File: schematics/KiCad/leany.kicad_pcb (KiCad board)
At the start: 2 copper layers, 108.3 x 71.6 mm, 61 parts, among them J1 SWD, J2 ST7735S, J3 USB C, Q1 AO3401A, Q2 DMG6601LVT-7, SW1 BOOT_MODE, SW2 ZERO, SW3 HOLD, SW4 POWER, U1 LSM6DSO, U2 STM32F103C8Tx, U3 CH340C, U4 AP2112K-3.3, U5 BQ25619, Y1 8MHz

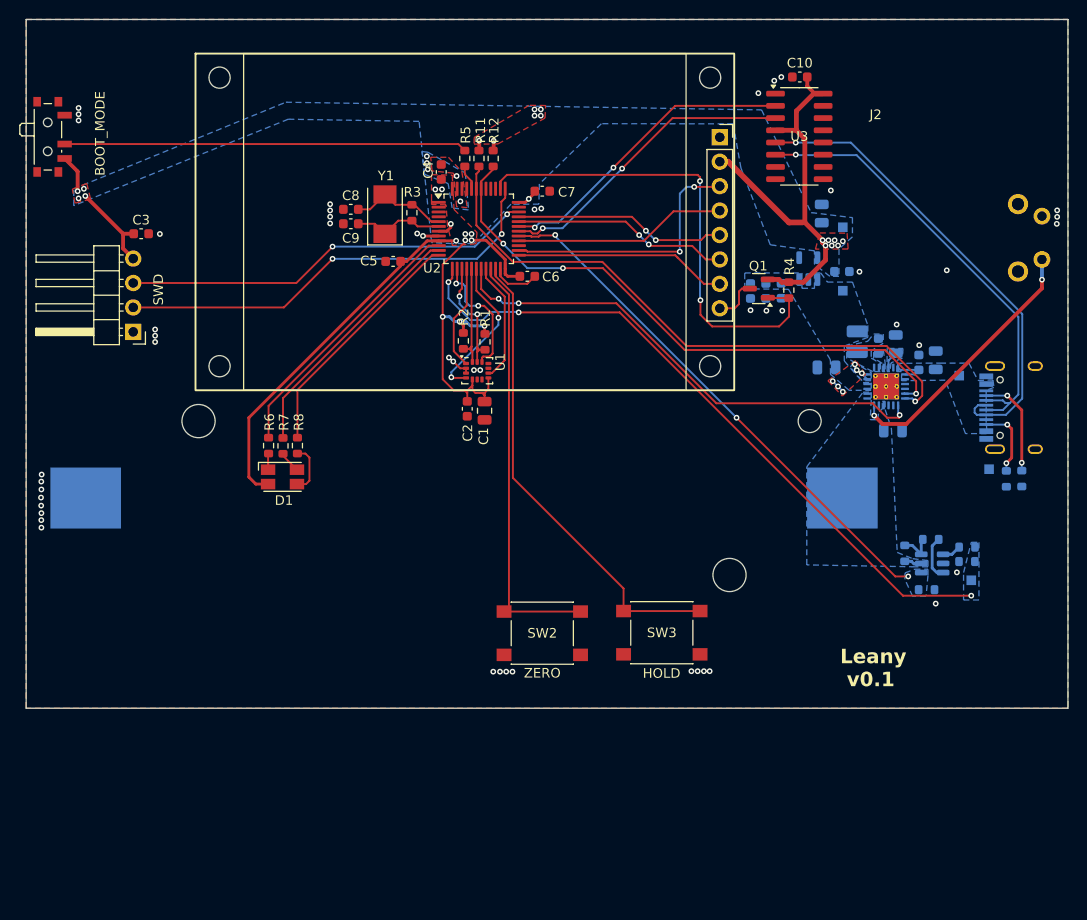
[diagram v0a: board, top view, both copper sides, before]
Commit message: redesign layout and power management
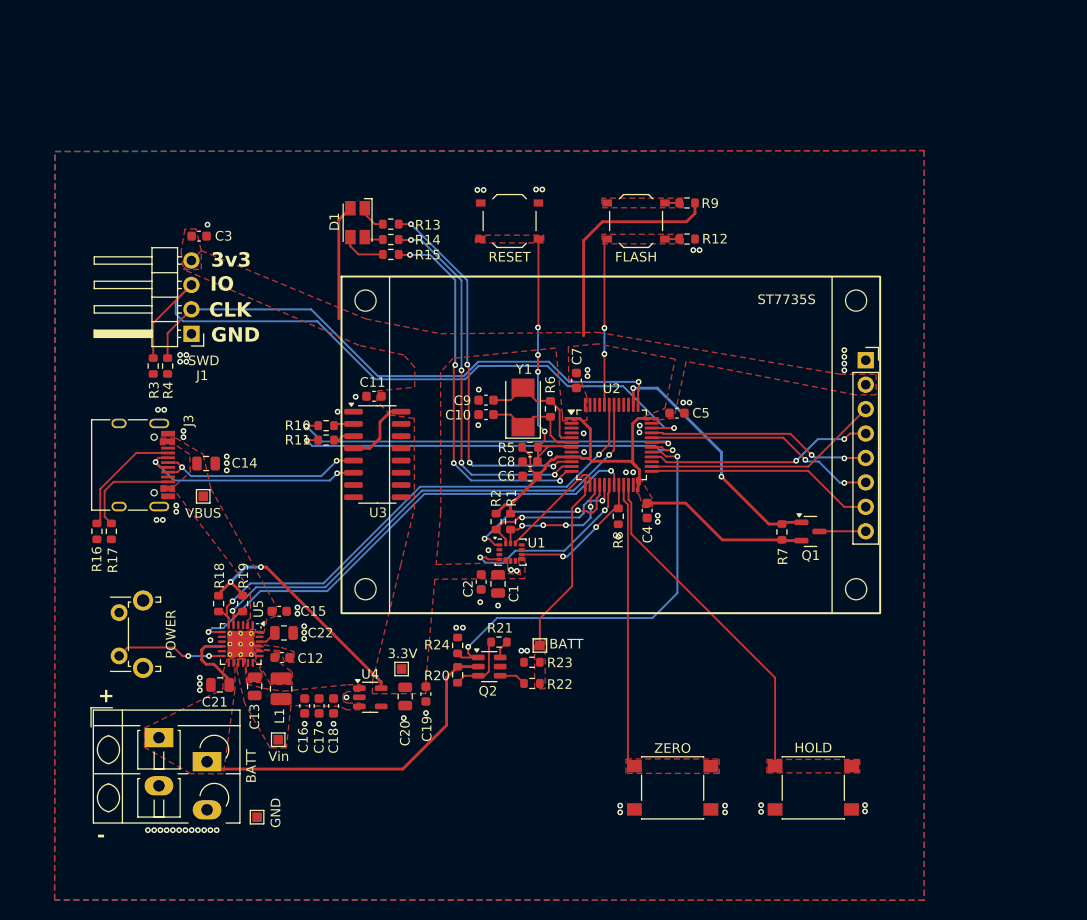
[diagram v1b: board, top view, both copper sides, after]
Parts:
- removed BT1: Battery, Battery:BatteryHolder_Keystone_1042_1x18650
- added C22: 4.7u, Capacitor_SMD:C_0805_2012Metric, F.Cu at (116.2, 119.8)
- added J4: BATT, TerminalBlock_WAGO:TerminalBlock_WAGO_804-102_1x02_P5.00mm_45Degree, F.Cu at (103.2, 130.7)
- added R18: 4.7k, Resistor_SMD:R_0603_1608Metric, F.Cu at (109.5, 116.8)
- added R19: 4.7k, Resistor_SMD:R_0603_1608Metric, F.Cu at (112.0, 116.8)
- added R20: 10k, Resistor_SMD:R_0603_1608Metric, F.Cu at (134.3, 124.2)
- added R21: 10k, Resistor_SMD:R_0603_1608Metric, F.Cu at (138.6, 120.8)
- added R22: 56k, Resistor_SMD:R_0603_1608Metric, F.Cu at (142.0, 125.0)
- added R23: 56k, Resistor_SMD:R_0603_1608Metric, F.Cu at (142.0, 122.8)
- added R24: 100k, Resistor_SMD:R_0603_1608Metric, F.Cu at (134.3, 121.1)
- added SW5: POWER, Button_Switch_THT:SW_Tactile_SPST_Angled_PTS645Vx31-2LFS, F.Cu at (99.1, 122.2)
- C10: value 100n -> 20p
- C11: value 47n -> 100n; moved to F.Cu
- C12: value 10u -> 47n; footprint Capacitor_SMD:C_0805_2012Metric -> Capacitor_SMD:C_0603_1608Metric; moved to F.Cu
- C13: value 22u -> 10u; moved to F.Cu
- C14: value 1u -> 22u; footprint Capacitor_SMD:C_0603_1608Metric -> Capacitor_SMD:C_0805_2012Metric; moved to F.Cu
- C15: value 22n -> 1u; moved to F.Cu
- C16: value 100n -> 22n; moved to F.Cu
- C17: value 1u -> 100n; moved to F.Cu
- C18, C20, J3, L1, Q2, TP1, TP2, TP3, TP4, U4, U5: moved to F.Cu
- C19: value 10u -> 1u; footprint Capacitor_SMD:C_0805_2012Metric -> Capacitor_SMD:C_0603_1608Metric; moved to F.Cu
- C21: value 4.7u -> 10u; moved to F.Cu
- C8: value 20p -> 1u
- R10: value 5.1k -> 4k7; moved to F.Cu
- R11: value 4.7k -> 4k7
- R12: value 4.7k -> 100k
- R13, R14: value 10k -> 820R; moved to F.Cu
- R15: value 56k -> 820R; moved to F.Cu
- R16: value 56k -> 5.1k; moved to F.Cu
- R17: value 100k -> 5.1k; moved to F.Cu
- R3: value 1M -> 10k
- R4: value 18k -> 10k
- R5: value 100k -> 10k
- R6: value 820R -> 1M
- R7: value 820R -> 18k
- R8: value 820R -> 100k
- R9: value 5.1k -> 10k; moved to F.Cu
- SW1: value BOOT_MODE -> RESET; footprint Button_Switch_SMD:SW_SPDT_PCM12 -> Button_Switch_SMD:SW_Push_1P1T_XKB_TS-1187A
- SW2: value ZERO -> FLASH; footprint leany_footprints:SW_Push_1P1T_NO_6x6mm_H9.5mm -> Button_Switch_SMD:SW_Push_1P1T_XKB_TS-1187A
- SW3: value HOLD -> ZERO
- SW4: value POWER -> HOLD; footprint Button_Switch_THT:SW_Tactile_SPST_Angled_PTS645Vx31-2LFS -> leany_footprints:SW_Push_1P1T_NO_6x6mm_H9.5mm; moved to F.Cu
- TP5: value BATT+ -> BATT; moved to F.Cu
- moved J3 93.3 mm to (100.2, 102.3)
- moved R16 90.5 mm to (96.8, 109.2), turned to -90 degrees
- moved R17 85.0 mm to (98.3, 109.2), turned to -90 degrees
- moved TP4 84.3 mm to (113.5, 138.9), turned to 0 degrees
- moved TP2 79.6 mm to (107.8, 105.6), turned to 0 degrees
- moved C21 78.7 mm to (109.6, 125.2), turned to 180 degrees
- moved C13 78.5 mm to (113.2, 125.3)
- moved TP1 75.0 mm to (115.7, 130.9), turned to 0 degrees
- moved C14 74.8 mm to (108.2, 102.2), turned to 0 degrees
- moved U5 72.2 mm to (111.8, 121.0), turned to -90 degrees
- moved R10 70.9 mm to (120.6, 98.2), turned to 0 degrees
- moved L1 69.9 mm to (116.0, 125.6), turned to -90 degrees
- moved C18 69.5 mm to (121.4, 127.4), turned to -90 degrees
- moved R15 67.2 mm to (127.3, 80.5), turned to 0 degrees
- moved R4 65.1 mm to (104.2, 92.0), turned to -90 degrees
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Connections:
- C10 pad 1: +3V3 -> GND
- C10 pad 2: GND -> Net-(U2-PD1)
- C11 pad 1: Net-(C11-Pad1) -> +3V3
- C11 pad 2: Net-(U5-BTST) -> GND
- C12 pad 1: SYS -> Net-(C12-Pad1)
- C12 pad 2: GND -> Net-(U5-BTST)
- C13 pad 1: Net-(U5-PSEL) -> SYS
- C15 pad 1: SYS -> Net-(U5-PSEL)
- C18 pad 1: +3V3 -> SYS
- C20 pad 1: +BATT -> +3V3
- C21 pad 1: Net-(U5-REGN) -> +BATT
- C8 pad 2: Net-(U2-PD0) -> Net-(U2-NRST)
- C9 pad 2: Net-(U2-PD1) -> Net-(U2-PD0)
- L1 pad 1: Net-(C11-Pad1) -> Net-(C12-Pad1)
- R10 pad 1: Net-(J3-CC2) -> /FTDI_RX
- R10 pad 2: GND -> Net-(U3-TXD)
- R11 pad 1: CHG_SDA -> /FTDI_TX
- R11 pad 2: +3V3 -> Net-(U3-RXD)
- R12 pad 1: CHG_SCL -> /BOOT0
- R12 pad 2: +3V3 -> GND
- R13 pad 1: Net-(Q2B-G) -> Net-(D1-RK)
- R13 pad 2: +BATT -> /LED_RED
- R14 pad 1: Net-(Q2B-G) -> Net-(D1-GK)
- R14 pad 2: Net-(Q2A-D) -> /LED_GREEN
- R15 pad 1: BATT_VOLT -> Net-(D1-BK)
- R15 pad 2: Net-(Q2B-D) -> /LED_BLUE
- R16 pad 1: GND -> Net-(J3-CC1)
- R16 pad 2: BATT_VOLT -> GND
- R17 pad 1: BATT_EN -> Net-(J3-CC2)
- R3 pad 1: Net-(U2-PD0) -> /DEBUG_SWDIO
- R3 pad 2: Net-(U2-PD1) -> GND
- R4 pad 1: /ST7735S_BL -> /DEBUG_SWDCLK
- R4 pad 2: +3V3 -> GND
- R5 pad 1: /BOOT0 -> +3V3
- R5 pad 2: Net-(SW1-B) -> Net-(U2-NRST)
- R6 pad 1: Net-(D1-RK) -> Net-(U2-PD0)
- R6 pad 2: /LED_RED -> Net-(U2-PD1)
- R7 pad 1: Net-(D1-GK) -> /ST7735S_BL
- R7 pad 2: /LED_GREEN -> +3V3
- R8 pad 1: Net-(D1-BK) -> GND
- R8 pad 2: /LED_BLUE -> /LSM6DSO_INT2
- R9 pad 1: Net-(J3-CC1) -> +3V3
- R9 pad 2: GND -> Net-(R9-Pad2)
- SW1 pad 2: Net-(SW1-B) -> Net-(U2-NRST)
- SW2 pad 1: Net-(U2-PB10) -> Net-(R9-Pad2)
- SW2 pad 2: GND -> /BOOT0
- SW3 pad 1: GND -> Net-(U2-PB10)
- SW3 pad 2: Net-(U2-PB11) -> GND
- SW4 pad 1: Net-(U5-~{QON}) -> GND
- SW4 pad 2: GND -> Net-(U2-PB11)
- U2 pad 7: +3V3 -> Net-(U2-NRST)
- U3 pad 2: /FTDI_RX -> Net-(U3-TXD)
- U3 pad 3: /FTDI_TX -> Net-(U3-RXD)
- U5 pad 19: Net-(C11-Pad1) -> Net-(C12-Pad1)
- U5 pad 20: Net-(C11-Pad1) -> Net-(C12-Pad1)
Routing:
- net BATT_VOLT: track 71.1 -> 18.6 mm, vias 3 -> 0
- net Net-(SW1-B): track 41.9 -> 0.00 mm
- net +BATT: track 2.17 -> 42.8 mm
- net /DEBUG_SWDIO: track 43.2 -> 73.1 mm, vias 2 -> 1
- net Net-(U2-NRST): track 0.00 -> 29.4 mm, vias 0 -> 4
- net USB_D+: track 50.3 -> 22.2 mm, vias 1 -> 2
- net /ST7735S_BL: track 50.5 -> 26.6 mm
- net USB_D-: track 46.8 -> 24.8 mm, vias 1 -> 2
- net +3V3: track 143.0 -> 123.5 mm, vias 29 -> 2
- net Net-(U5-~{QON}): track 27.7 -> 11.4 mm
- net /BOOT0: track 2.61 -> 18.8 mm, vias 0 -> 2
- net Net-(U2-PB10): track 44.6 -> 29.7 mm
- net /LED_BLUE: track 25.4 -> 39.7 mm, vias 0 -> 4
- net Net-(U2-PB11): track 49.0 -> 35.5 mm
- net GND: track 13.3 -> 0.00 mm, vias 62 -> 88
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- added copper zone on F.Cu, net +BATT
- added copper zone on F.Cu, net /BOOT0
- added copper zone on F.Cu, net BATT_VOLT
- added copper zone on F.Cu, net Net-(C12-Pad1)
- added copper zone on F.Cu, net Net-(R9-Pad2)
- added copper zone on F.Cu, net Net-(U2-NRST)
- added copper zone on F.Cu, net Net-(U2-PB10)
- added copper zone on F.Cu, net Net-(U2-PB11)
- added copper zone on F.Cu, net Net-(U5-BTST)
- added copper zone on F.Cu, net Net-(U5-PSEL)
- added copper zone on F.Cu, net SYS
- removed copper zone on B.Cu, net +3V3
- removed copper zone on B.Cu, net +BATT
- removed copper zone on B.Cu, net BATT_EN
- removed copper zone on B.Cu, net BATT_VOLT
- removed copper zone on B.Cu, net Net-(C11-Pad1)
- removed copper zone on B.Cu, net Net-(U5-BTST)
- removed copper zone on B.Cu, net Net-(U5-PSEL)
- removed copper zone on B.Cu, net Net-(U5-REGN)
- removed copper zone on B.Cu, net SYS
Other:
- board outline removed
- board text added: "+"
- board text added: "-"
- board text added: "3v3"
- board text added: "CLK"
- board text added: "GND"
- board text added: "IO"
- board text removed: "Leany"
- board text removed: "v0.1"

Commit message: add ST7735S pins silkscreen Improve layout
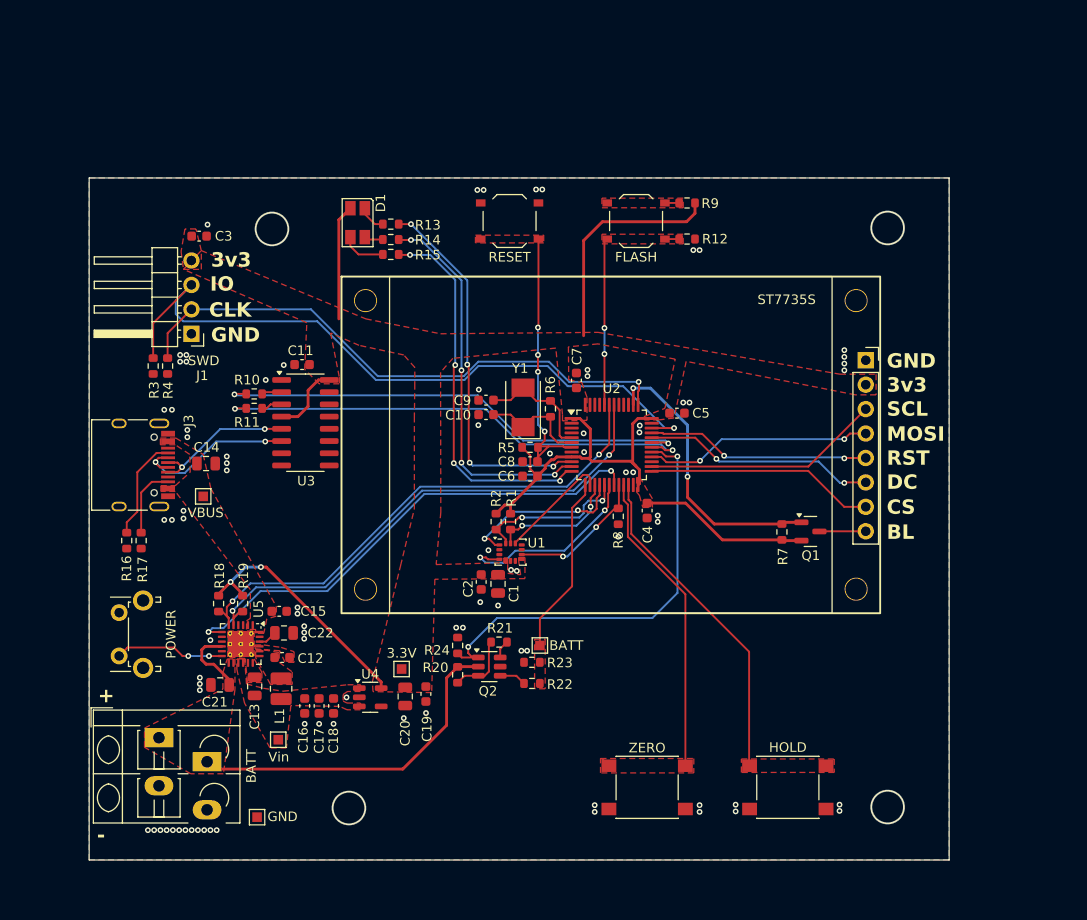
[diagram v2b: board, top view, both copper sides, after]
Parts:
- D1: footprint LED_SMD:LED_Avago_PLCC4_3.2x2.8mm_CW -> leany_footprints:LED_Avago_PLCC4_3.2x2.8mm_CW
- TP1, TP2, TP3, TP4, TP5: footprint TestPoint:TestPoint_Pad_1.0x1.0mm -> leany_footprints:TestPoint_Pad_1.0x1.0mm
- Y1: footprint Crystal:Crystal_SMD_Abracon_ABM3-2Pin_5.0x3.2mm -> leany_footprints:Crystal_SMD_Abracon_ABM3-2Pin_5.0x3.2mm
- moved U3 8.17 mm to (118.5, 97.9)
- moved C11 8.17 mm to (118.1, 91.9)
- moved R10 8.17 mm to (113.2, 95.0)
- moved R11 8.17 mm to (113.2, 96.5)
- moved R16 3.25 mm to (99.9, 110.2)
- moved R17 3.25 mm to (101.4, 110.2)
- moved SW3 2.65 mm to (154.0, 135.8)
- moved SW4 2.65 mm to (168.6, 135.8)
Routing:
- net /FTDI_RX: track 41.3 -> 50.3 mm
- net /FTDI_TX: track 41.9 -> 50.7 mm
- net USB_D+: track 22.2 -> 15.3 mm
- net USB_D-: track 24.8 -> 18.0 mm
- net Net-(J3-CC2): track 10.7 -> 7.43 mm
- net Net-(U2-PB10): track 29.7 -> 32.8 mm
- net /ST7735S_BL: track 26.6 -> 29.5 mm
- net Net-(J3-CC1): track 12.3 -> 10.8 mm
- net Net-(U2-PB11): track 35.5 -> 34.4 mm
- net /LSM6DSO_SCL: track 13.9 -> 13.5 mm, vias 4 -> 2
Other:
- board outline added: 89.4 x 70.9 mm
- board text added: "BL"
- board text added: "CS"
- board text added: "DC"
- board text added: "MOSI"
- board text added: "RST"
- board text added: "SCL"

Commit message: Fix BTSNS add README
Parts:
- added C23: 100n, Capacitor_SMD:C_0805_2012Metric, F.Cu at (106.3, 119.1)
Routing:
- net +BATT: track 42.8 -> 45.5 mm

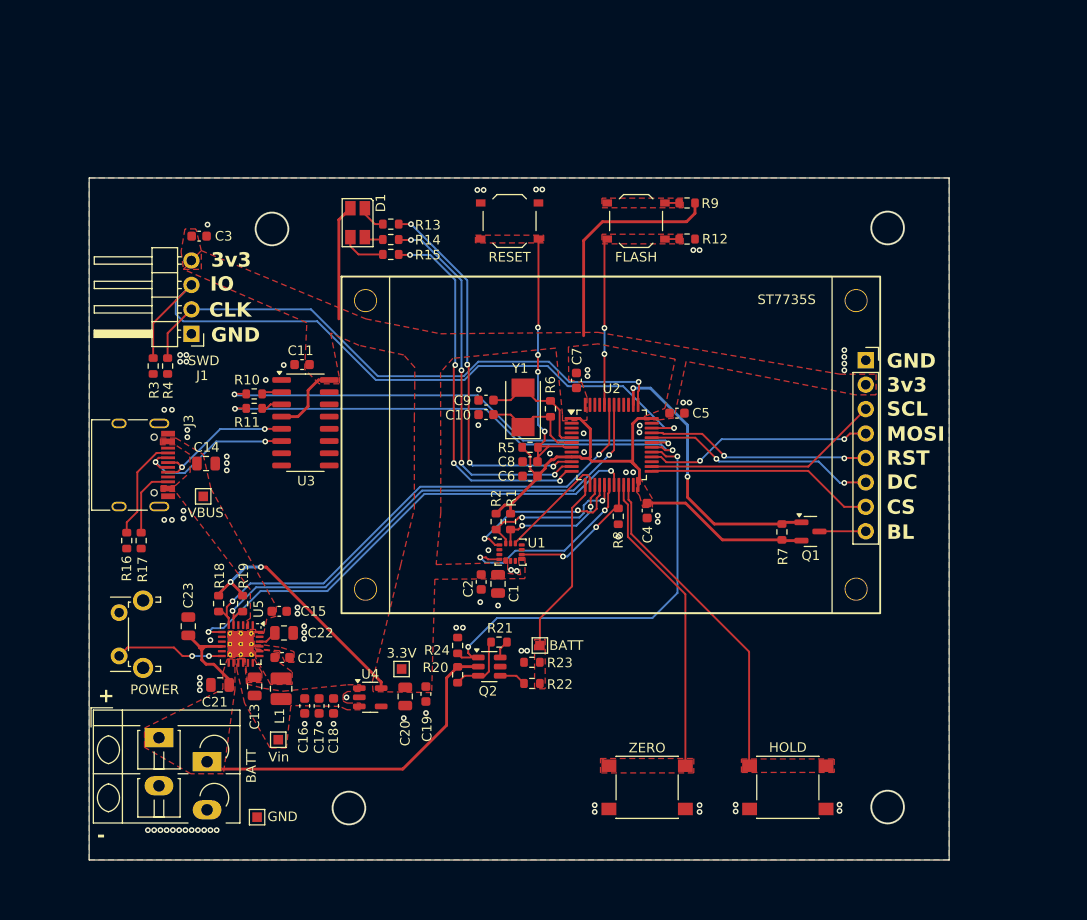
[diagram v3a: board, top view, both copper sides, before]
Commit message: update JLCPCB BOM source a wago connector to replace the battery holder
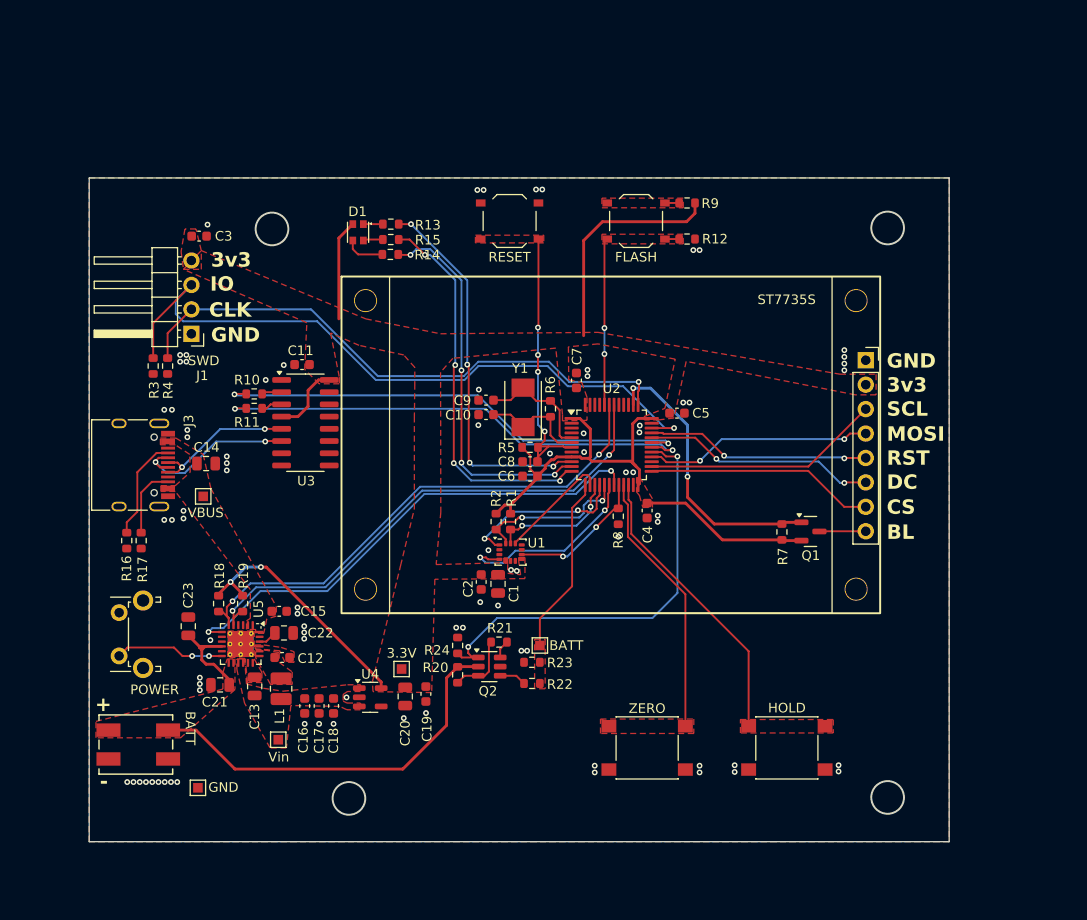
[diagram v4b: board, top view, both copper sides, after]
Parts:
- removed J4: BATT, TerminalBlock_WAGO:TerminalBlock_WAGO_804-102_1x02_P5.00mm_45Degree
- added J5: BATT, leany_footprints:Wago_2059-302_998-403, F.Cu at (100.8, 131.4)
- D1: value ASMB-MTB1-0B3A2 -> NH-B2020RGBA-HF; footprint leany_footprints:LED_Avago_PLCC4_3.2x2.8mm_CW -> leany_footprints:NH-B2020RGBA-HF
- R16, R17: value 5.1k -> 5k1
- R18, R19: value 4.7k -> 4k7
- moved TP4 6.86 mm to (107.3, 135.9)
- moved SW4 4.10 mm to (168.5, 131.8)
- moved SW3 4.10 mm to (154.0, 131.8)
- moved R14 1.55 mm to (127.3, 80.5)
- moved R15 1.55 mm to (127.3, 78.9)
- moved D1 1.00 mm to (124.0, 78.2), turned to 90 degrees
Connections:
- D1 pad 2: Net-(D1-GK) -> Net-(D1-BK)
- D1 pad 3: Net-(D1-BK) -> +3V3
- D1 pad 4: +3V3 -> Net-(D1-GK)
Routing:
- net +BATT: track 45.5 -> 50.9 mm
- net Net-(U2-PB10): track 32.8 -> 28.7 mm
- net Net-(U2-PB11): track 34.4 -> 30.3 mm
- net Net-(D1-BK): track 4.68 -> 2.07 mm
- net Net-(D1-GK): track 1.98 -> 4.20 mm
- net +3V3: track 123.5 -> 121.9 mm
- net Net-(D1-RK): track 2.91 -> 2.03 mm
- net /LED_BLUE: track 39.7 -> 40.4 mm
- net GND: vias 88 -> 85
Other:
- board size 89.4 x 70.9 mm -> 89.4 x 69 mm

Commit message: Improve layout
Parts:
- removed J5: BATT, leany_footprints:Wago_2059-302_998-403
- added J4: BATT, leany_footprints:wago_2060-452_998-404, F.Cu at (103.7, 132.1)
- R13: value 820R -> 220R
- R14, R15: value 820R -> 150R
- moved TP4 13.3 mm to (120.6, 136.4)
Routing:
- net +BATT: track 50.9 -> 45.9 mm
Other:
- outline, holes or cut-outs redrawn
- board text added: "0.2"
- board text added: "0.75"
- board text added: "18"
- board text added: "24"
- board text added: "7mm"
- board text added: "9mm"
- board text added: "AWG"
- board text added: "Battery connector wiring"
- board text added: "Max"
- board text added: "Min."
- board text added: "Stripping"
- board text added: "leany rev 0.2"
- board text added: "mm²"
